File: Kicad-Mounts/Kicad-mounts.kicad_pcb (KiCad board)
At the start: 2 copper layers, 29 x 36 mm, 10 parts, among them P1 CONN_10, P2 CONN_10, P3 CONN_6X2, P6 CONN_3, U2 TPS77033

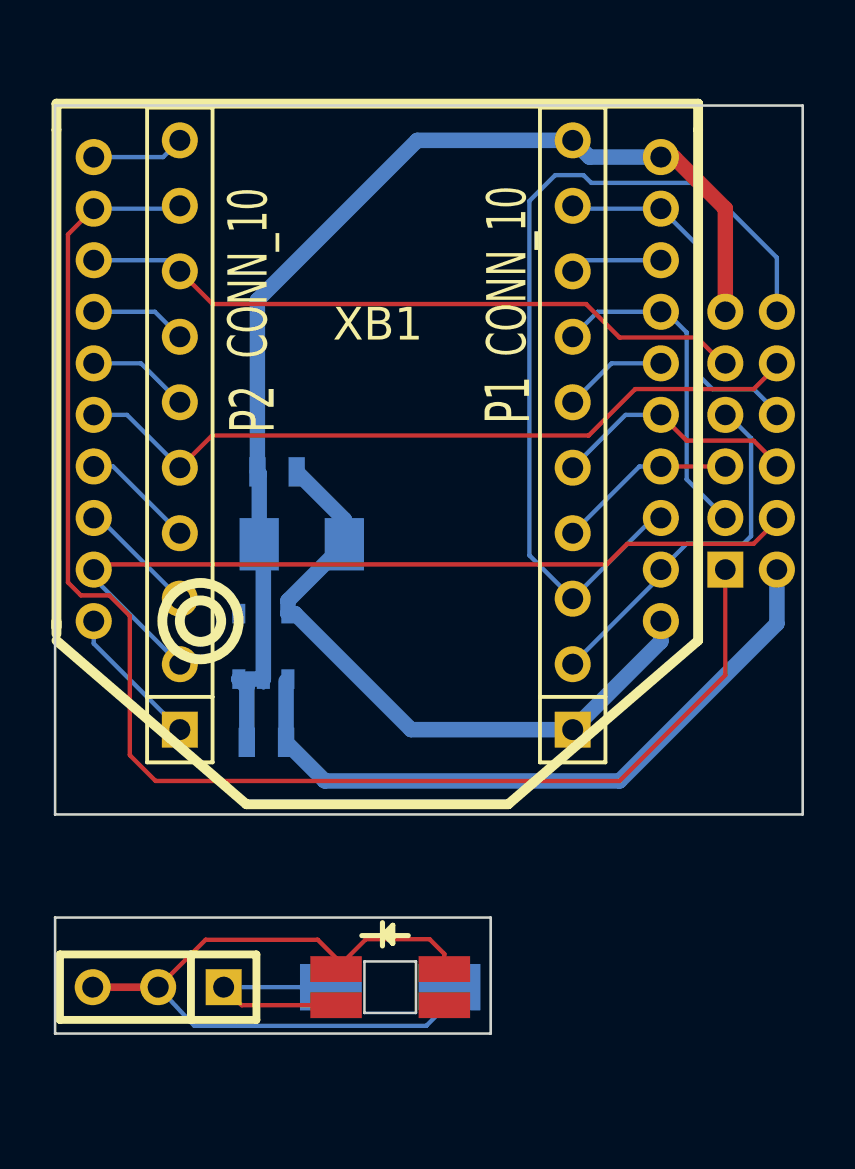
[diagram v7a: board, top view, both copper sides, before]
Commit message: Create version 4 of the XBee mount board and modify the main board to allow the XBee base to sit on the main board.
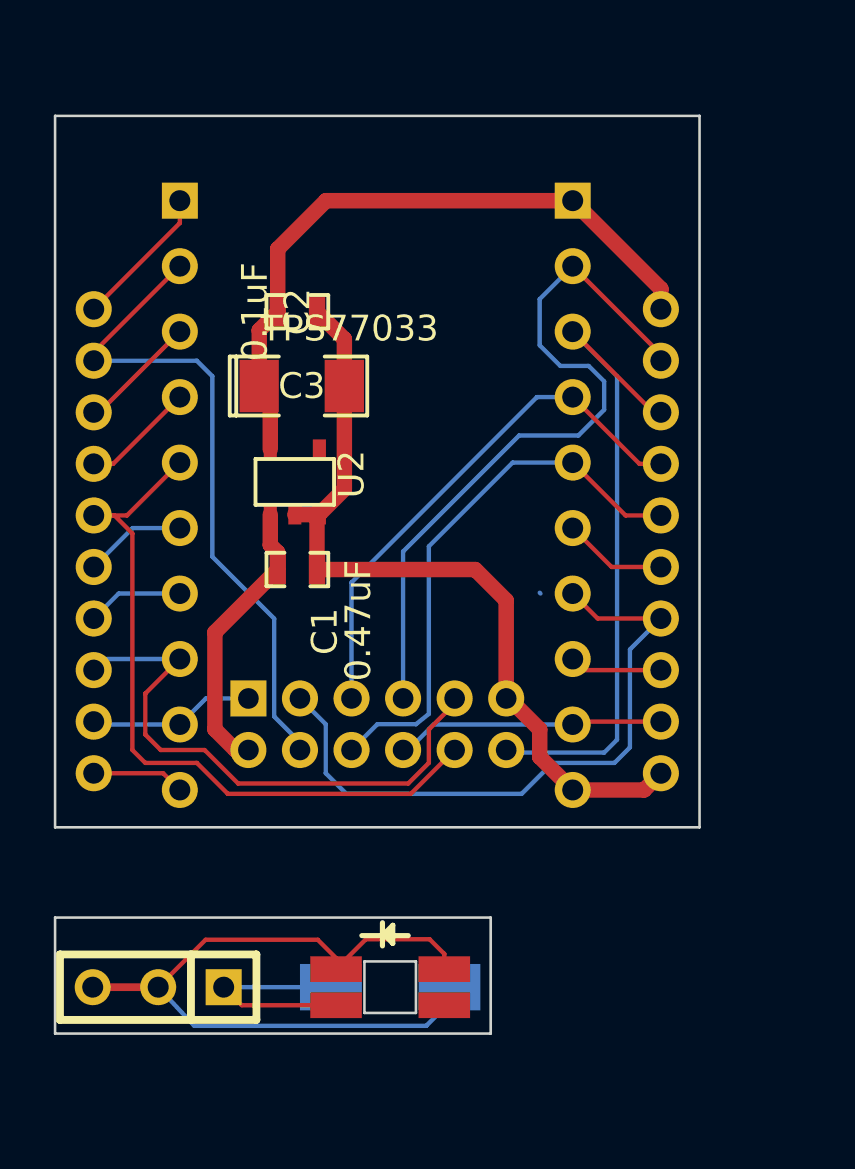
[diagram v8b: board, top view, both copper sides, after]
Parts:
- C1, C2, C3, U2: moved to F.Cu
- P1, P2, XB1: moved to B.Cu
- moved P3 18.2 mm to (180.5, 114.0), turned to 0 degrees
- moved XB1 12.1 mm to (180.5, 97.9)
- moved C1 6.81 mm to (177.4, 108.0), turned to 0 degrees
- moved U2 6.50 mm to (177.3, 104.6), turned to 0 degrees
- moved C2 6.26 mm to (177.4, 98.0), turned to 0 degrees
- moved C3 6.14 mm to (177.6, 100.9), turned to 0 degrees
- moved P1 2.34 mm to (188.1, 105.1), turned to 270 degrees
- moved P2 2.34 mm to (172.8, 105.1), turned to 270 degrees
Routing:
- net /CTS: track 56.2 -> 6.90 mm
- net VCC: track 27.1 -> 11.1 mm
- net /Rx: track 14.3 -> 28.6 mm
- net /Reset: track 6.99 -> 20.6 mm
- net GND: track 44.5 -> 31.7 mm
- net /Bootloader: track 13.0 -> 25.8 mm
- net /XBee-Reset: track 9.66 -> 21.3 mm
- net /Tx: track 34.3 -> 25.8 mm
- net /VBatt: track 32.4 -> 26.1 mm
- net /On/Sleep: track 26.8 -> 23.3 mm
- net /Sleep_Rq: track 14.5 -> 11.3 mm
- net /RTS: track 29.1 -> 28.3 mm
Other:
- board size 29 x 36 mm -> 25 x 35.6 mm
